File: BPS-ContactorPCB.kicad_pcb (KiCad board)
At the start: 2 copper layers, 3 parts, among them J1 Conn_01x04, J2 Conn_01x04, J3 Conn_01x02

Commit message: done
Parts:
- removed the J3 at (127.5, 100.7)
- added J2: E-STOP, UTSVT_Connectors:Molex_MicroFit3.0_1x2xP3.00mm_PolarizingPeg_Vertical, F.Cu at (128.2, 89.1)
- added J4: Contactor - No Sense, UTSVT_Connectors:Molex_MicroFit3.0_1x4xP3.00mm_PolarizingPeg_Vertical, F.Cu at (125.0, 110.8)
- added REF**: MountingHole_3.2mm_M3, MountingHole:MountingHole_3.2mm_M3, F.Cu at (142.2, 76.1)
- added REF**: MountingHole_3.2mm_M3, MountingHole:MountingHole_3.2mm_M3, F.Cu at (116.3, 76.1)
- added REF**: MountingHole_3.2mm_M3, MountingHole:MountingHole_3.2mm_M3, F.Cu at (116.3, 113.3)
- added REF**: MountingHole_3.2mm_M3, MountingHole:MountingHole_3.2mm_M3, F.Cu at (142.2, 113.3)
- J1: value Conn_01x04 -> BPS_IN
- J3: renamed from J2; value Conn_01x04 -> Contactor - Sense
- moved J3 9.90 mm to (125.0, 99.4)
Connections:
- J3 pad 1: /CONTACTOR_V+ -> /ESTOP
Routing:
- net /ESTOP: track 0.00 -> 24.3 mm
- net /AUX_1: track 10.8 -> 26.0 mm
- net /AUX_2: track 10.8 -> 24.9 mm
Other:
- board outline added: 32.8 x 44.4 mm

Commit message: Added 2nd ESTOP
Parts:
- added J3: ESTOP, UTSVT_Connectors:Molex_MicroFit3.0_1x2xP3.00mm_PolarizingPeg_Vertical, F.Cu at (134.9, 89.0)
- J2: value E-STOP -> ESTOP
- moved J2 7.78 mm to (120.4, 89.0)
- renumbered J3 to J4, J4 to J5
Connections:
- J2 pad 2: /ESTOP -> /ESTOP_1
- J4 pad 1: /ESTOP -> /ESTOP_2
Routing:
- net /ESTOP_2: track 0.00 -> 16.0 mm
- net /ESTOP: track 24.3 -> 11.4 mm
- net /ESTOP_1: track 0.00 -> 11.5 mm
- net /AUX_1: track 26.0 -> 21.4 mm
- net /AUX_2: track 24.9 -> 21.4 mm

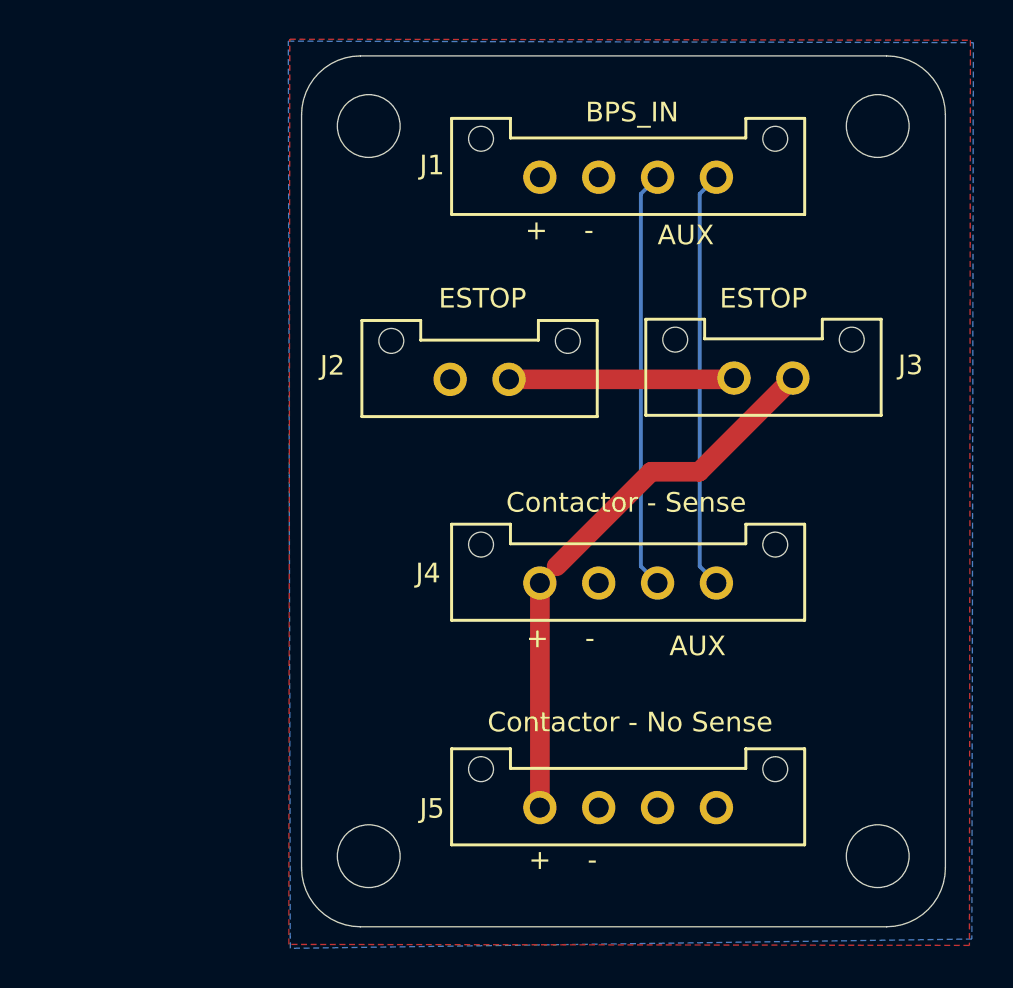
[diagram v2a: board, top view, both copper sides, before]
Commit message: updated layout
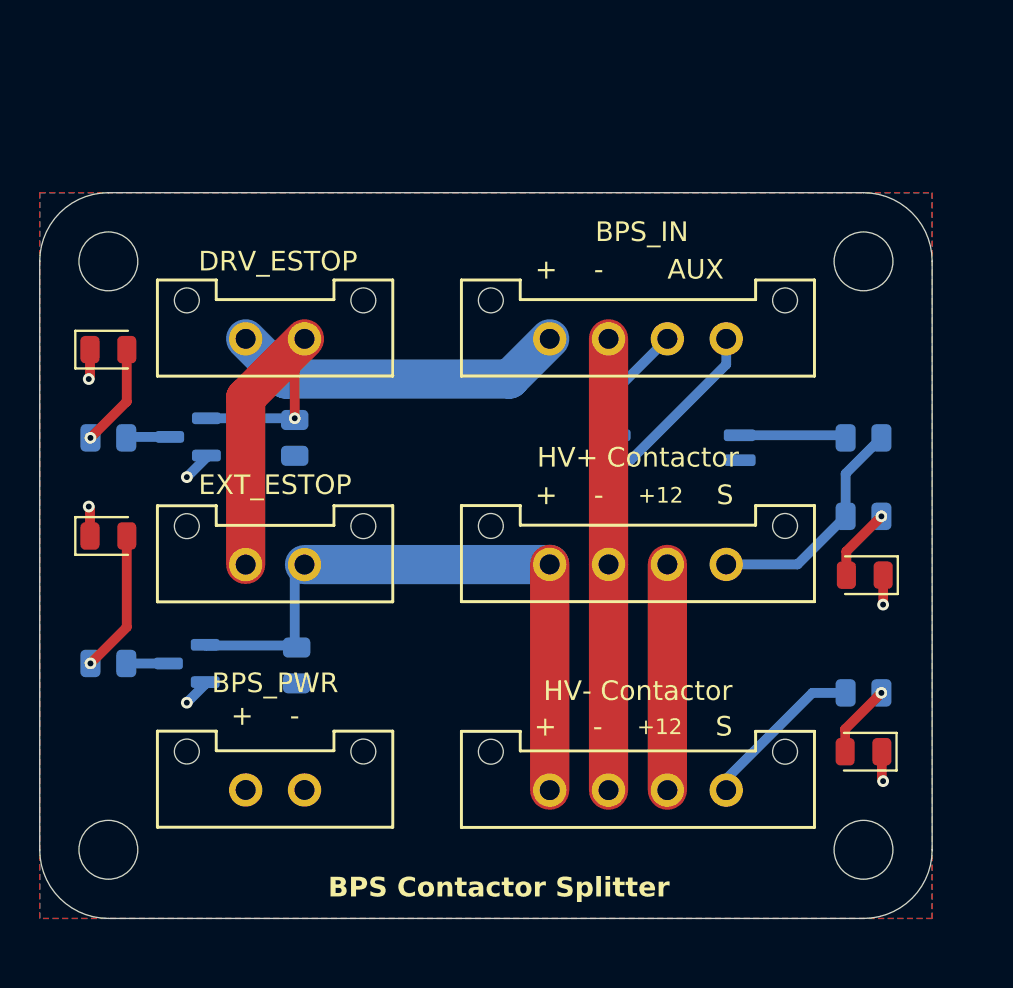
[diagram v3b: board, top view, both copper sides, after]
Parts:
- removed REF** (x4): MountingHole_3.2mm_M3, MountingHole:MountingHole_3.2mm_M3
- added D1: Contactor 1, LED_SMD:LED_0805_2012Metric, F.Cu at (141.6, 99.0)
- added D2: Contactor 2, LED_SMD:LED_0805_2012Metric, F.Cu at (141.5, 108.0)
- added D3: ExtEStop, LED_SMD:LED_0805_2012Metric, F.Cu at (103.0, 97.0)
- added D4: DrvEStop, LED_SMD:LED_0805_2012Metric, F.Cu at (103.0, 87.5)
- added H1: M3, MountingHole:MountingHole_3mm, F.Cu at (103.0, 83.0)
- added H2: M3, MountingHole:MountingHole_3mm, F.Cu at (103.0, 113.0)
- added H3: M3, MountingHole:MountingHole_3mm, F.Cu at (141.5, 83.0)
- added H4: M3, MountingHole:MountingHole_3mm, F.Cu at (141.5, 113.0)
- added J1: BPS_PWR, UTSVT_Connectors:Molex_MicroFit3.0_1x2xP3.00mm_PolarizingPeg_Vertical, F.Cu at (110.0, 110.0)
- added LOGO2: Logo_Placeholder, UTSVT_Special:Hallock_Image_Tiny, B.Cu at (119.4, 108.3)
- added Q1: PMV35EPER, Package_TO_SOT_SMD:SOT-23, B.Cu at (107.0, 103.5)
- added Q2: PMV35EPER, Package_TO_SOT_SMD:SOT-23, B.Cu at (107.1, 92.0)
- added R1: 510, Resistor_SMD:R_0805_2012Metric, B.Cu at (141.5, 92.0)
- added R2: 1.5k, Resistor_SMD:R_0805_2012Metric, B.Cu at (141.5, 96.0)
- added R3: 1.5k, Resistor_SMD:R_0805_2012Metric, B.Cu at (141.5, 105.0)
- added R4: 1.5k, Resistor_SMD:R_0805_2012Metric, B.Cu at (103.0, 103.5)
- added R5: 10k, Resistor_SMD:R_0805_2012Metric, B.Cu at (112.6, 103.6)
- added R6: 1.5k, Resistor_SMD:R_0805_2012Metric, B.Cu at (103.0, 92.0)
- added R7: 10k, Resistor_SMD:R_0805_2012Metric, B.Cu at (112.5, 92.0)
- added U1: EL3H7, Package_SO:SOP-4_4.4x2.6mm_P1.27mm, B.Cu at (132.0, 92.5)
- J3: renamed from J2; value ESTOP -> DRV_ESTOP
- J4: renamed from J3; value ESTOP -> EXT_ESTOP
- J5: renamed from J4; value Contactor - Sense -> HV+ Contactor
- J6: renamed from J5; value Contactor - No Sense -> HV- Contactor
- moved J4 26.7 mm to (110.0, 98.5)
- moved J3 10.6 mm to (110.0, 87.0)
- moved J2 8.26 mm to (125.5, 87.0)
- moved J5 1.07 mm to (125.5, 98.5)
- moved J6 1.02 mm to (125.5, 110.0)
- renumbered J1 to J2
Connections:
- net /ESTOP_1 renamed /DRV_ESTOP
- J2 pad 3: /AUX_1 -> /BPS_AUX_1
- J2 pad 4: /AUX_2 -> /BPS_AUX_2
- J4 pad 2: /ESTOP_2 -> /EXT_ESTOP
- J5 pad 1: /ESTOP_2 -> /EXT_ESTOP
- J5 pad 3: /AUX_1 -> +12V
- J5 pad 4: /AUX_2 -> /C1_SENSE
- J6 pad 1: /ESTOP -> /EXT_ESTOP
- J6 pad 3: unconnected-(J5-Pin_3-Pad3) -> +12V
- J6 pad 4: unconnected-(J5-Pin_4-Pad4) -> /C2_SENSE
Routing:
- net /EXT_ESTOP: track 0.00 -> 33.1 mm
- net /CONTACTOR_V-: track 0.00 -> 23.0 mm
- net /AUX_2: track 21.4 -> 0.00 mm
- net /AUX_1: track 21.4 -> 0.00 mm
- net /CONTACTOR_V+: track 0.00 -> 17.2 mm
- net /ESTOP_2: track 16.0 -> 0.00 mm
- net +12V: track 0.00 -> 14.5 mm, vias 0 -> 2
- net /C1_SENSE: track 0.00 -> 11.9 mm
- net /ESTOP: track 11.4 -> 0.00 mm
- net /DRV_ESTOP: track 11.5 -> 21.5 mm, vias 0 -> 1
- net /BPS_AUX_2: track 0.00 -> 9.02 mm
- net /C2_SENSE: track 0.00 -> 8.47 mm
- net Net-(D3-A): track 0.00 -> 7.27 mm, vias 0 -> 1
- net GNDPWR: track 0.00 -> 6.08 mm, vias 0 -> 4
- net /BPS_AUX_1: track 0.00 -> 6.03 mm
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- added copper zone on F.Cu, net +12V
- added copper zone on B.Cu, net GNDPWR
- removed copper zone on F.Cu, net /CONTACTOR_V+
- removed copper zone on B.Cu, net /CONTACTOR_V-
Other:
- board size 32.8 x 44.4 mm -> 45.5 x 37 mm
- board text added: "+12"
- board text added: "BPS Contactor Splitter"
- board text added: "S"
